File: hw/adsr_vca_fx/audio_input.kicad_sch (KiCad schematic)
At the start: 12 parts, among them J1 Conn_01x02, U1 TL972, U2 MCP603-xCH, U3 MCP603-xCH, U6 TL972

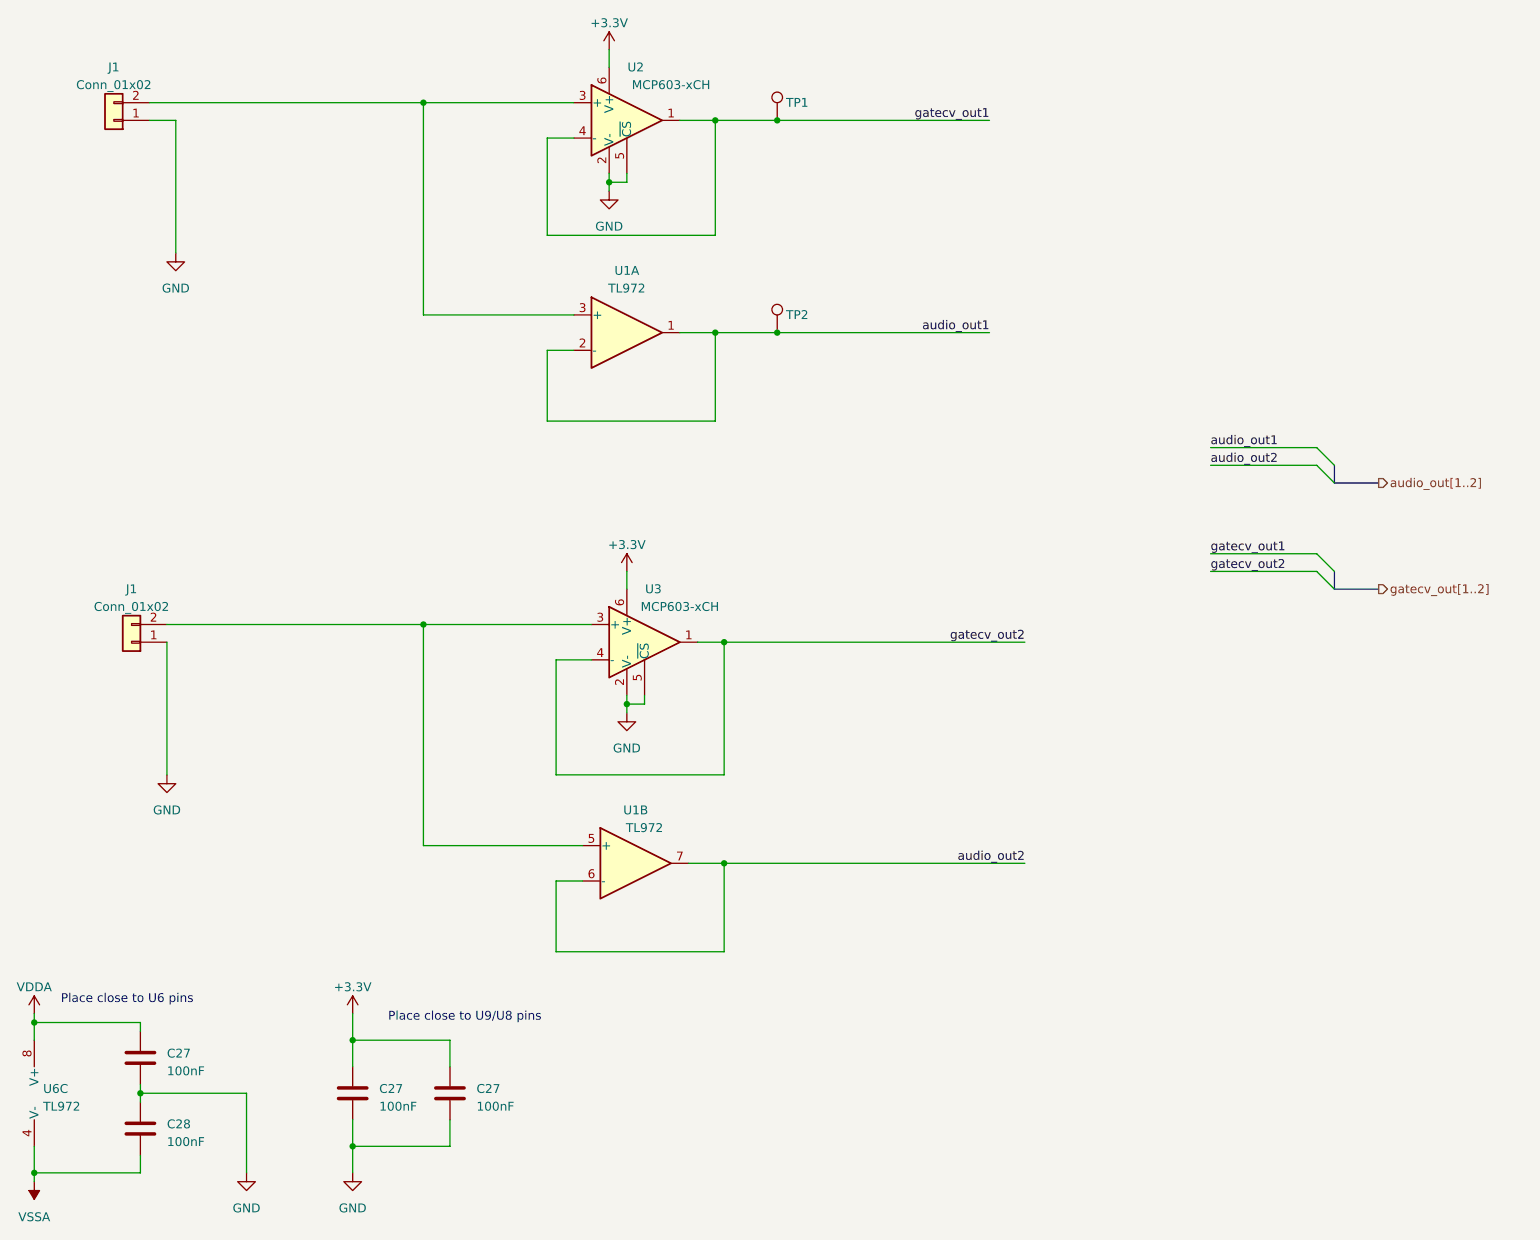
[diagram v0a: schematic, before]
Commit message: modified design into normal/inverted envlope
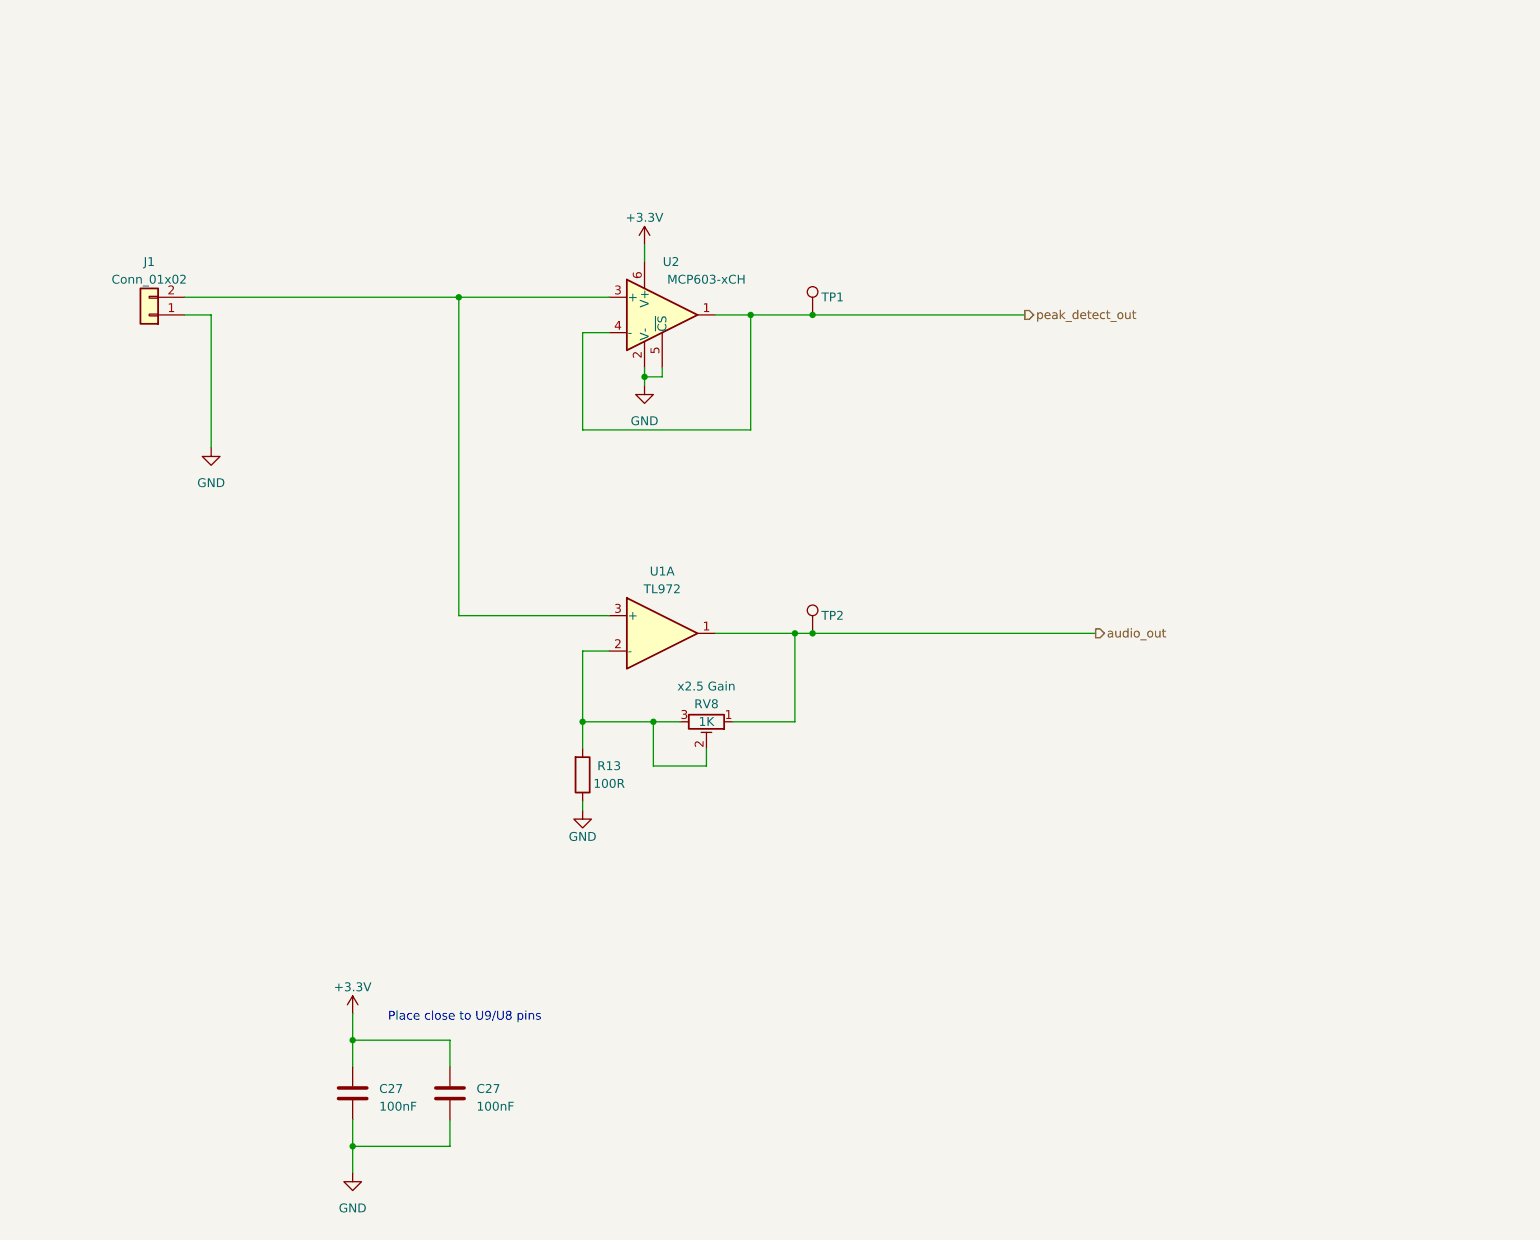
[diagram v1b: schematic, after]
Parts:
- removed C27, C28: 100nF, Capacitor_SMD:C_0805_2012Metric_Pad1.18x1.45mm_HandSolder, symbol Device:C
- removed J1: Conn_01x02, Connector_PinHeader_2.54mm:PinHeader_1x02_P2.54mm_Vertical, symbol Connector_Generic:Conn_01x02
- removed unit 2 of U1
- removed U3: MCP603-xCH, Package_TO_SOT_SMD:SOT-23-6, symbol Amplifier_Operational:MCP603-xCH
- removed U6: TL972, Package_SO:SOIC-8_3.9x4.9mm_P1.27mm, symbol Amplifier_Operational:TL072
- added R13: 100R, Resistor_SMD:R_0805_2012Metric_Pad1.20x1.40mm_HandSolder, symbol Device:R
- added RV8: 1K, Potentiometer_THT:Potentiometer_Piher_PT-10-V10_Vertical, symbol Device:R_Potentiometer_Trim
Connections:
- net GND: now also R13.1
- net audio_out1 renamed audio_out
- net audio_out: now also RV8.1; no longer U1.2 (-)
- net gatecv_out1 renamed peak_detect_out
- new net: R13.2, RV8.2, RV8.3, U1.2 (-)
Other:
- note removed: "Place close to U6 pins"
- moved on the sheet: J1, TP1, TP2, U1A, U2

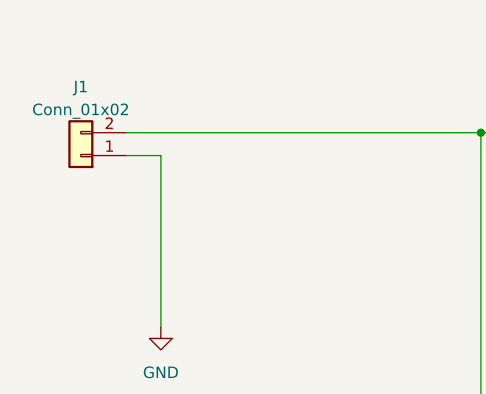
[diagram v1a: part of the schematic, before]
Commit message: updated text labels
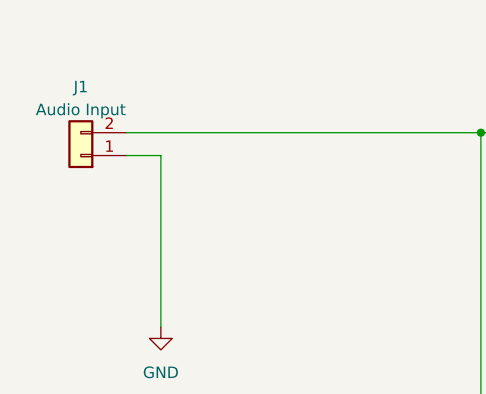
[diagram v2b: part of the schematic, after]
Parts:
- J1: value Conn_01x02 -> Audio Input
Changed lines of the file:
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@@
       (effects (font (size 1.27 1.27)))
     )
-    (property "Value" "Conn_01x02" (at 73.66 55.88 0)
+    (property "Value" "Audio Input" (at 73.66 55.88 0)
       (effects (font (size 1.27 1.27)))
     )

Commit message: first draft layout
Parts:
- C27: value 100nF -> 1uF
- RV8: footprint Potentiometer_THT:Potentiometer_Piher_PT-10-V10_Vertical -> Potentiometer_THT:Potentiometer_Runtron_RM-065_Vertical
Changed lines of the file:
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@@
       (effects (font (size 1.27 1.27)))
     )
-    (property "Footprint" "Potentiometer_THT:Potentiometer_Piher_PT-10-V10_Vertical" (at 153.67 119.38 0)
+    (property "Footprint" "Potentiometer_THT:Potentiometer_Runtron_RM-065_Vertical" (at 153.67 119.38 0)
       (effects (font (size 1.27 1.27)) hide)
     )
@@
         )
         (path "/2c7cc946-dcca-4ffb-b6a0-bf0c9ddb491b/0d7fbd8f-e081-47cd-87b5-dfbc75ed6757"
-          (reference "RV10") (unit 1)
+          (reference "RV1") (unit 1)
         )
       )
@@
   (symbol (lib_id "power:GND") (at 82.55 80.01 0) (unit 1)
     (in_bom yes) (on_board yes) (dnp no) (fields_autoplaced)
-    (property "Reference" "#PWR010" (at 82.55 86.36 0)
+    (property "Reference" "#PWR012" (at 82.55 86.36 0)
       (effects (font (size 1.27 1.27)) hide)
     )
@@
       (project "adsr_vca_fx"
         (path "/2c7cc946-dcca-4ffb-b6a0-bf0c9ddb491b/0d7fbd8f-e081-47cd-87b5-dfbc75ed6757"
-          (reference "#PWR010") (unit 1)
+          (reference "#PWR012") (unit 1)
         )
       )
@@
         )
         (path "/2c7cc946-dcca-4ffb-b6a0-bf0c9ddb491b/0d7fbd8f-e081-47cd-87b5-dfbc75ed6757"
-          (reference "#PWR021") (unit 1)
+          (reference "#PWR015") (unit 1)
         )
       )
@@
         )
         (path "/2c7cc946-dcca-4ffb-b6a0-bf0c9ddb491b/0d7fbd8f-e081-47cd-87b5-dfbc75ed6757"
-          (reference "R21") (unit 1)
+          (reference "R1") (unit 1)
         )
       )
@@
       (effects (font (size 1.27 1.27)) (justify left))
     )
-    (property "Value" "100nF" (at 120.65 174.625 0)
+    (property "Value" "1uF" (at 120.65 174.625 0)
       (effects (font (size 1.27 1.27)) (justify left))
     )
@@
         )
         (path "/2c7cc946-dcca-4ffb-b6a0-bf0c9ddb491b/0d7fbd8f-e081-47cd-87b5-dfbc75ed6757"
-          (reference "#PWR015") (unit 1)
+          (reference "#PWR014") (unit 1)
         )
       )
@@
   (symbol (lib_id "power:+3.3V") (at 102.87 161.29 0) (unit 1)
     (in_bom yes) (on_board yes) (dnp no) (fields_autoplaced)
-    (property "Reference" "#PWR014" (at 102.87 165.1 0)
+    (property "Reference" "#PWR013" (at 102.87 165.1 0)
       (effects (font (size 1.27 1.27)) hide)
     )
@@
       (project "adsr_vca_fx"
         (path "/2c7cc946-dcca-4ffb-b6a0-bf0c9ddb491b/0d7fbd8f-e081-47cd-87b5-dfbc75ed6757"
-          (reference "#PWR014") (unit 1)
-        )
-      )
+          (reference "#PWR013") (unit 1)
+        )
+      )
